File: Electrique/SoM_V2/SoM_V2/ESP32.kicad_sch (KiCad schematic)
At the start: 15 parts, among them Q601 MBT3904DW1T1G, SW601 SW_BOOT, SW602 SW_CHIP_EN, U601 ESP32-S3-MINI-1U, U602 74HC238

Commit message: push pour frank
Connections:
- net GND: now also U602.4 (~{E1}), U602.5 (~{E2})
- net Vcc_3V3: no longer U602.4 (~{E1}), U602.5 (~{E2})
- no-connect marks 10 -> 8
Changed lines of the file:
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@@
-	)
-	(junction
-		(at 143.51 63.5)
-		(diameter 0)
-		(color 0 0 0 0)
 	)
 	(junction
@@
 	)
 	(junction
-		(at 143.51 66.04)
-		(diameter 0)
-		(color 0 0 0 0)
-	)
-	(junction
 		(at 45.72 40.64)
 		(diameter 0)
@@
 	)
 	(junction
+		(at 139.7 66.04)
+		(diameter 0)
+		(color 0 0 0 0)
+	)
+	(junction
 		(at 172.72 34.29)
 		(diameter 0)
@@
 	)
 	(no_connect
-		(at 143.51 63.5)
-	)
-	(no_connect
 		(at 107.95 60.96)
 	)
@@
 	)
 	(no_connect
-		(at 143.51 66.04)
-	)
-	(no_connect
 		(at 107.95 76.2)
 	)
@@
 	(wire
 		(pts
-			(xy 143.51 66.04) (xy 143.51 68.58)
-		)
-		(stroke
-			(width 0)
-			(type default)
-		)
-	)
-	(wire
-		(pts
 			(xy 30.48 40.64) (xy 30.48 45.72)
 		)
@@
 	(wire
 		(pts
+			(xy 139.7 66.04) (xy 143.51 66.04)
+		)
+		(stroke
+			(width 0)
+			(type default)
+		)
+	)
+	(wire
+		(pts
 			(xy 114.3 48.26) (xy 107.95 48.26)
 		)
@@
 	(wire
 		(pts
+			(xy 139.7 63.5) (xy 139.7 66.04)
+		)
+		(stroke
+			(width 0)
+			(type default)
+		)
+	)
+	(wire
+		(pts
 			(xy 271.78 91.44) (xy 271.78 82.55)
 		)
@@
 	(wire
 		(pts
+			(xy 143.51 63.5) (xy 139.7 63.5)
+		)
+		(stroke
+			(width 0)
+			(type default)
+		)
+	)
+	(wire
+		(pts
 			(xy 92.71 22.86) (xy 92.71 29.21)
 		)
@@
 	(wire
 		(pts
-			(xy 143.51 58.42) (xy 143.51 63.5)
+			(xy 143.51 73.66) (xy 143.51 68.58)
 		)
 		(stroke
@@
 		(pts
 			(xy 172.72 41.91) (xy 182.88 41.91)
-		)
-		(stroke
-			(width 0)
-			(type default)
-		)
-	)
-	(wire
-		(pts
-			(xy 143.51 63.5) (xy 143.51 66.04)
 		)
 		(stroke
@@
 	(global_label "Vcc_3V3"
 		(shape input)
-		(at 143.51 58.42 180)
+		(at 143.51 73.66 180)
 		(fields_autoplaced yes)
 		(effects
@@
 		)
 		(property "Intersheetrefs" "${INTERSHEET_REFS}"
-			(at 132.7838 58.42 0)
+			(at 132.7838 73.66 0)
 			(effects
 				(font
@@
 					(unit 1)
 				)
+			)
+		)
+	)
+	(symbol
+		(lib_id "power:GND")
+		(at 139.7 66.04 0)
+		(unit 1)
+		(exclude_from_sim no)
+		(in_bom yes)
+		(on_board yes)
+		(dnp no)
+		(property "Reference" "#PWR0608"
+			(at 139.7 72.39 0)
+			(effects
+				(font
+					(size 1.27 1.27)
+				)
+				(hide yes)
+			)
+		)
+		(property "Value" "GND"
+			(at 139.7 69.85 0)
+			(effects
+				(font
+					(size 1.27 1.27)
+				)
+			)
+		)
+		(property "Footprint" ""
+			(at 139.7 66.04 0)
+			(effects
+				(font
+					(size 1.27 1.27)
+				)
+				(hide yes)
+			)
+		)
+		(property "Datasheet" ""
+			(at 139.7 66.04 0)
+			(effects
+				(font
+					(size 1.27 1.27)
+				)
+				(hide yes)
+			)
+		)
+		(property "Description" "Power symbol creates a global label with name \"GND\" , ground"
+			(at 139.7 66.04 0)
+			(effects
+				(font
+					(size 1.27 1.27)
+				)
+				(hide yes)
+			)
+		)
+		(pin "1"
+		)
+		(instances
+			(project "SoM_V2"
+				(path "/ecd44d9a-8113-48e2-a5bb-0de07ce8b9ce/42eddecc-5d06-4740-ba8f-a05813435351"
+					(reference "#PWR0608")
+					(unit 1)
+				)

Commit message: push fix ???
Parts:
- removed C604: 1µF, Resistor_SMD:R_0805_2012Metric, symbol Device:C
- removed C605: 0.1µF, Resistor_SMD:R_0805_2012Metric, symbol Device:C
- removed U602: 74HC238, Package_DFN_QFN:DHVQFN-16-1EP_2.5x3.5mm_P0.5mm_EP1x2mm, symbol 74xx:74HC238
- renumbered C601 to C501, C602 to C502, C603 to C503, C606 to C504, C607 to C505, Q601 to Q501, R601 to R501, R602 to R502, R603 to R503, SW601 to SW501, SW602 to SW502, U601 to U501
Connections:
- net CS_0 is gone; now on net SPI_CAN_ESP32: U501.8 (IO4)
- net GPIO47 is gone; now on net RESET_OTHERS: U501.27 (IO47)

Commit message: push v2.2
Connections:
- net RESET_OTHERS: no longer U501.15 (IO11)
- net CS_1 renamed GPIO5/TXD
- net SPI_CAN_ESP32 renamed GPIO4/RXD
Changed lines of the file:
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@@
 		)
 	)
-	(global_label "RESET_OTHERS"
-		(shape input)
-		(at 77.47 71.12 180)
-		(fields_autoplaced yes)
-		(effects
-			(font
-				(size 1.27 1.27)
-			)
-			(justify right)
-		)
-		(property "Intersheetrefs" "${INTERSHEET_REFS}"
-			(at 60.515 71.12 0)
+	(global_label "GPIO4{slash}RXD"
+		(shape input)
+		(at 77.47 53.34 180)
+		(fields_autoplaced yes)
+		(effects
+			(font
+				(size 1.27 1.27)
+			)
+			(justify right)
+		)
+		(property "Intersheetrefs" "${INTERSHEET_REFS}"
+			(at 63.72 53.34 0)
 			(effects
 				(font
@@
 		)
 	)
-	(global_label "CS_1"
+	(global_label "GPIO5{slash}TXD"
 		(shape input)
 		(at 77.47 55.88 180)
@@
 		)
 		(property "Intersheetrefs" "${INTERSHEET_REFS}"
-			(at 69.8282 55.88 0)
+			(at 64.0224 55.88 0)
 			(effects
 				(font
@@
 				(hide yes)
 			)
-		)
-	)
-	(global_label "SPI_CAN_ESP32"
-		(shape input)
-		(at 77.47 53.34 180)
-		(fields_autoplaced yes)
-		(effects
-			(font
-				(size 1.27 1.27)
-			)
-			(justify right)
-		)
-		(property "Intersheetrefs" "${INTERSHEET_REFS}"
-			(at 59.7287 53.34 0)
-			(effects
-				(font
-					(size 1.27 1.27)
-				)
-				(justify right)
-				(hide yes)
-			)

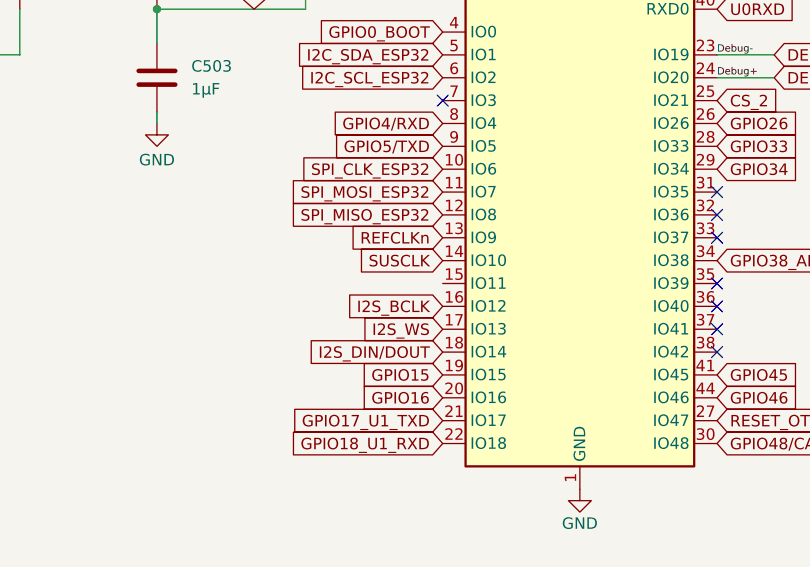
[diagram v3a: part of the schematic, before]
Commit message: push drc clean up, reste le silkscreen à faire
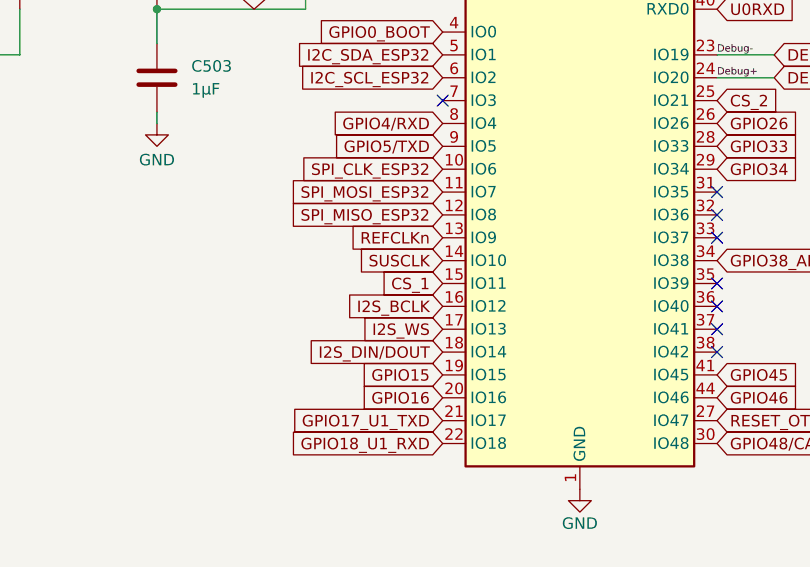
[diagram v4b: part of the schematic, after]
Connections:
- net CS_1: now reaches U501.15 (IO11)
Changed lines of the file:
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@@
+		)
+	)
+	(global_label "CS_1"
+		(shape input)
+		(at 77.47 71.12 180)
+		(fields_autoplaced yes)
+		(effects
+			(font
+				(size 1.27 1.27)
+			)
+			(justify right)
+		)
+		(property "Intersheetrefs" "${INTERSHEET_REFS}"
+			(at 69.8282 71.12 0)
+			(effects
+				(font
+					(size 1.27 1.27)
+				)
+				(justify right)
+				(hide yes)
+			)
 		)
 	)
